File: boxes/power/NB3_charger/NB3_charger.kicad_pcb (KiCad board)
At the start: 2 copper layers, 110 x 71 mm, 40 parts, among them J1 Barrel_Jack_PJ-036AH-SMT-TR, J2 Connector_S4B-PH-SM4-TB(LF)(S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, J3 Conn_01x02_Pin, SW1 SW_SPDT, U1 Voltage_Regulator_AP64501

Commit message: Work on PCBs (v1 and v2)
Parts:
- added H10: MountingHole, MountingHole:MountingHole_2.7mm_M2.5_ISO7380_Pad, F.Cu at (209.5, 46.2)
- added H11: MountingHole, MountingHole:MountingHole_2.7mm_M2.5_ISO7380_Pad, F.Cu at (209.5, 104.2)
- added H12: MountingHole, MountingHole:MountingHole_2.7mm_M2.5_ISO7380_Pad, F.Cu at (160.5, 104.2)
- added H13: MountingHole, MountingHole:MountingHole_2.7mm_M2.5_ISO7380_Pad, F.Cu at (154.5, 46.2)
- added H14: MountingHole, MountingHole:MountingHole_2.7mm_M2.5_ISO7380_Pad, F.Cu at (215.5, 46.2)
- added H5: MountingHole, MountingHole:MountingHole_2.7mm_M2.5_ISO7380_Pad, F.Cu at (144.0, 34.2)
- added H6: MountingHole, MountingHole:MountingHole_2.7mm_M2.5_ISO7380_Pad, F.Cu at (226.0, 34.2)
- added H7: MountingHole, MountingHole:MountingHole_2.7mm_M2.5_ISO7380_Pad, F.Cu at (226.0, 116.2)
- added H8: MountingHole, MountingHole:MountingHole_2.7mm_M2.5_ISO7380_Pad, F.Cu at (144.0, 116.2)
- added H9: MountingHole, MountingHole:MountingHole_2.7mm_M2.5_ISO7380_Pad, F.Cu at (160.5, 46.2)
- BT1, BT2, BT3, BT4, BT5, BT6: moved to F.Cu
- J2: value Connector_S4B-PH-SM4-TB(LF)(SN) -> B4B-PH-K-S; footprint NB3_charger:Connector_S4B-PH-SM4-TB(LF)(SN) -> NB3_charger:Connector_B4B-PH-K-S(LF)(SN)
- moved H3 121.3 mm to (236.0, 126.2), turned to 0 degrees
- moved H1 109.8 mm to (134.0, 24.2), turned to 0 degrees
- moved H2 103.0 mm to (236.0, 24.2), turned to 0 degrees
- moved BT1 86.2 mm to (227.0, 75.2), turned to -90 degrees
- moved BT6 86.0 mm to (143.0, 75.2), turned to -90 degrees
- moved SW1 79.2 mm to (173.0, 27.2), turned to 90 degrees
- moved R1 70.7 mm to (194.1, 23.4), turned to 180 degrees
- moved R6 69.1 mm to (200.0, 23.4), turned to 0 degrees
- moved D1 69.0 mm to (196.0, 24.2), turned to -90 degrees
- moved D2 68.4 mm to (198.0, 24.2), turned to -90 degrees
- moved J3 59.4 mm to (174.6, 45.0), turned to 180 degrees
- moved J1 56.5 mm to (185.3, 38.2), turned to -90 degrees
- moved C3 53.3 mm to (183.7, 42.2), turned to 180 degrees
- moved C1 50.5 mm to (183.7, 44.7), turned to 180 degrees
- moved C4 50.3 mm to (187.2, 42.2), turned to 0 degrees
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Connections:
- J2 pad 1: GND -> +5V
- J2 pad 2: GND -> +5V
- J2 pad 3: +5V -> GND
- J2 pad 4: +5V -> GND
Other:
- board size 110 x 71 mm -> 110 x 110 mm

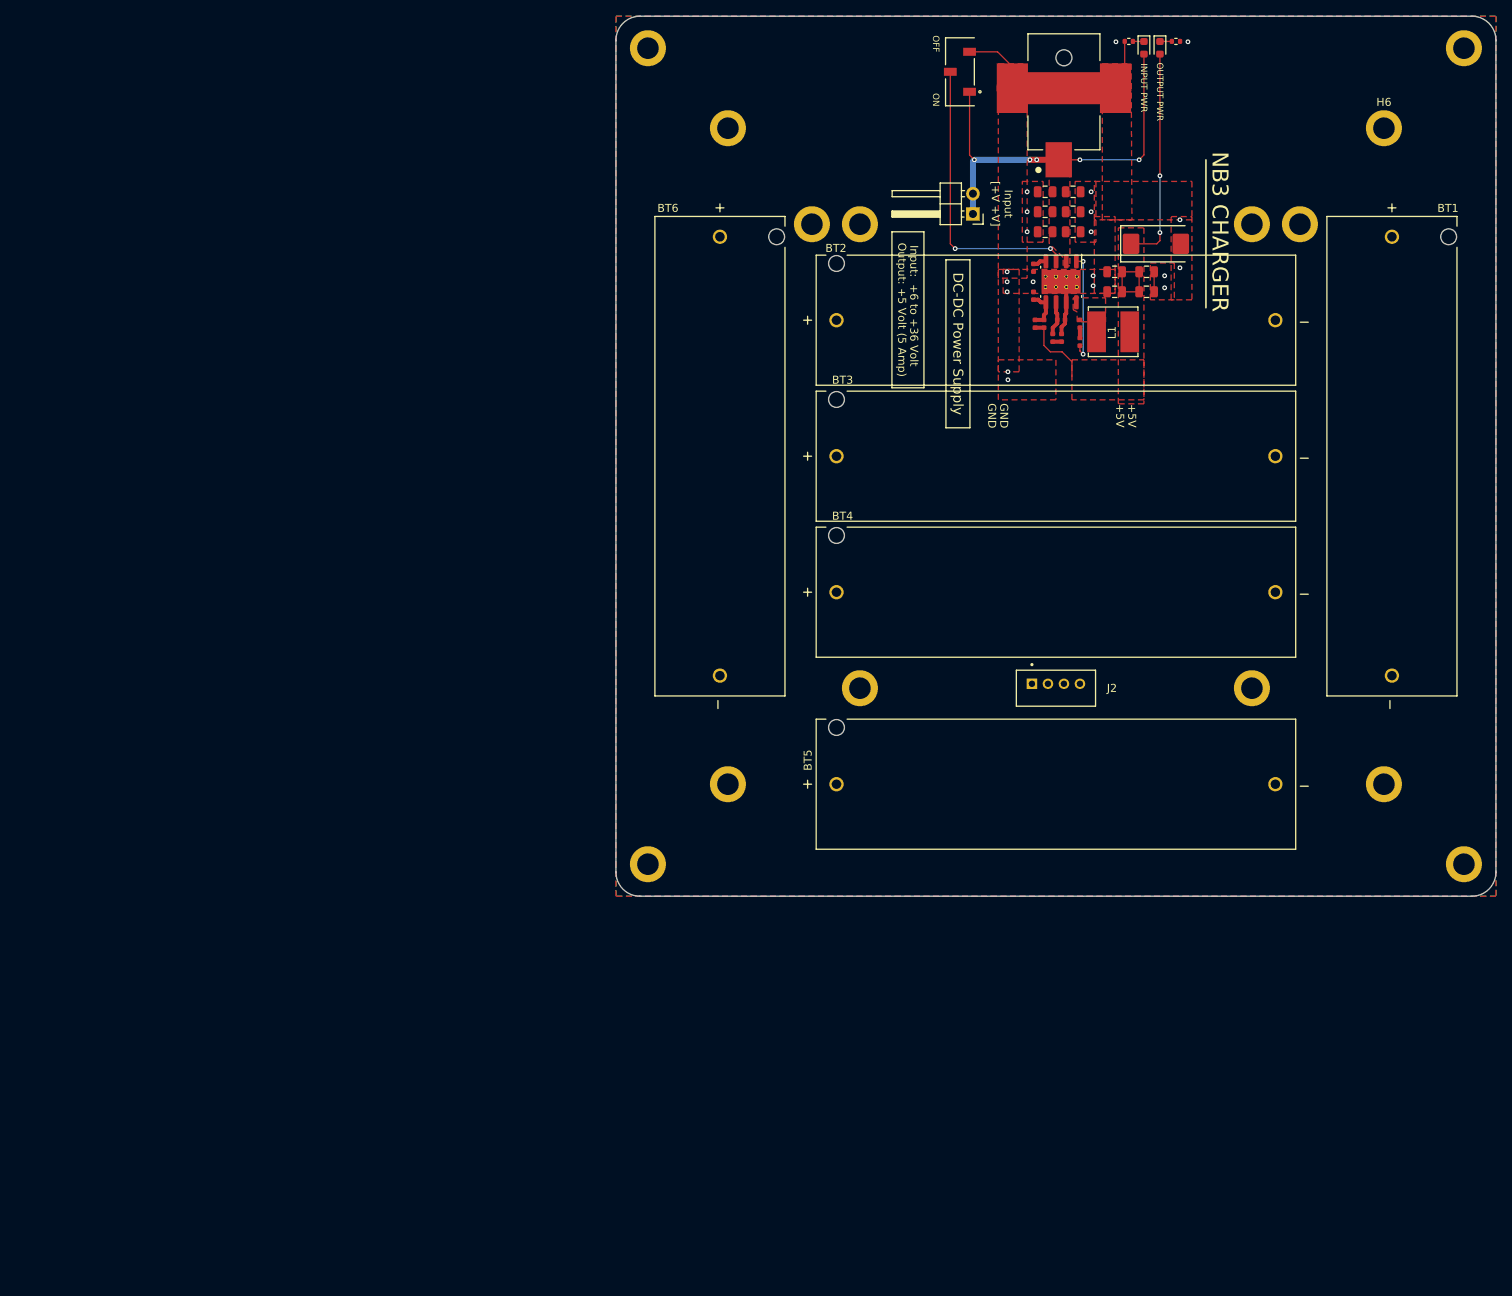
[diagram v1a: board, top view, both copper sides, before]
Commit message: PCB tweaks (charger and body)
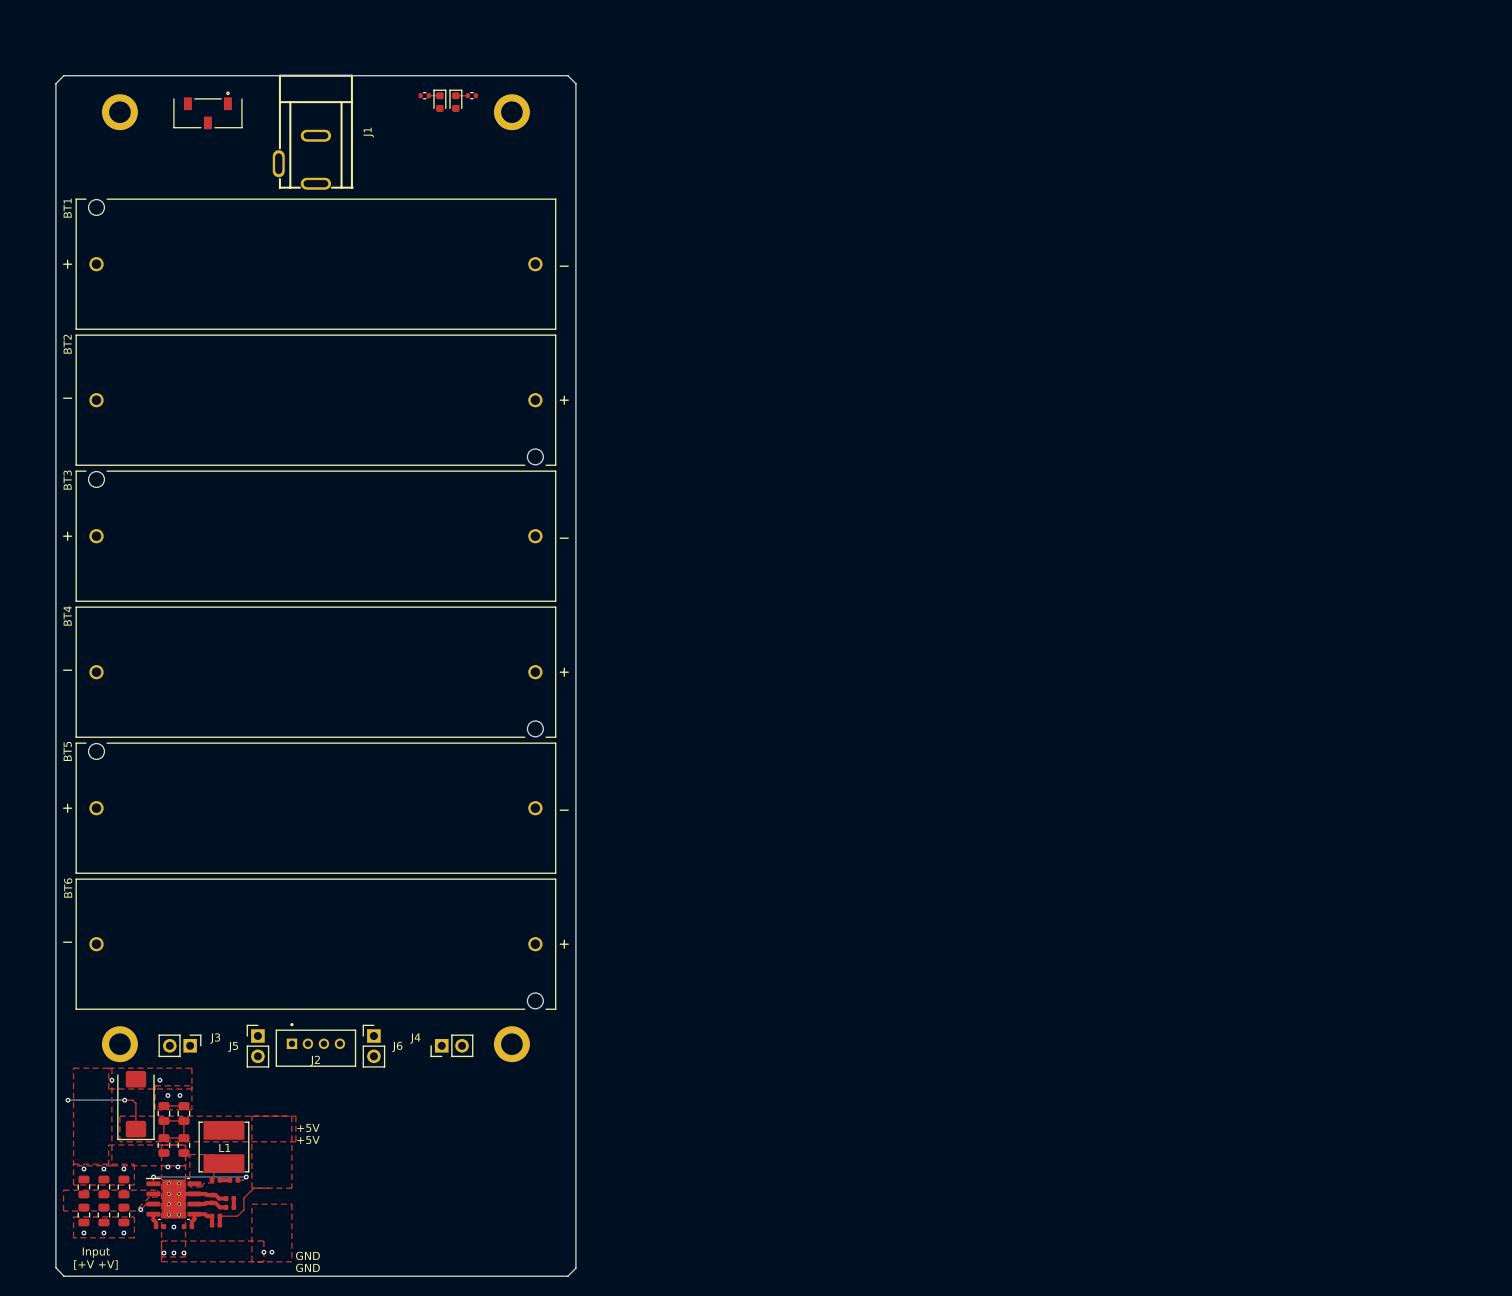
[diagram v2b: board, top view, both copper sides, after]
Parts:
- removed H1, H13, H14, H2, H3, H4, H5, H6, H7, H8: MountingHole, MountingHole:MountingHole_2.7mm_M2.5_ISO7380_Pad
- added J4: Conn_01x02_Pin, Connector_PinHeader_2.54mm:PinHeader_1x02_P2.54mm_Vertical, F.Cu at (108.2, 148.9)
- added J5: Conn_01x02_Pin, Connector_PinHeader_2.54mm:PinHeader_1x02_P2.54mm_Vertical, F.Cu at (85.2, 147.7)
- added J6: Conn_01x02_Pin, Connector_PinHeader_2.54mm:PinHeader_1x02_P2.54mm_Vertical, F.Cu at (99.8, 147.7)
- J1: value Barrel_Jack_PJ-036AH-SMT-TR -> Barrel_Jack-DC-5.5-2.1; footprint NB3_charger:Barrel_Jack_PJ-036AH-SMT-TR -> NB3_charger:Barrel_Jack_TH_XUNPU_DC-005-A200
- J3: footprint Connector_PinHeader_2.54mm:PinHeader_1x02_P2.54mm_Horizontal -> Connector_PinHeader_2.54mm:PinHeader_1x02_P2.54mm_Vertical
- moved C3 175.5 mm to (63.5, 170.1), turned to -90 degrees
- moved C4 175.4 mm to (63.5, 166.6), turned to 90 degrees
- moved C1 171.9 mm to (66.0, 170.1), turned to -90 degrees
- moved C5 171.9 mm to (66.0, 166.6), turned to 90 degrees
- moved C2 168.4 mm to (68.5, 170.1), turned to -90 degrees
- moved C6 168.3 mm to (68.5, 166.6), turned to 90 degrees
- moved C16 166.8 mm to (70.0, 156.2), turned to 90 degrees
- moved C8 162.1 mm to (73.0, 171.6), turned to 0 degrees
- moved C14 161.7 mm to (73.5, 157.4), turned to 90 degrees
- moved C13 161.4 mm to (73.5, 161.4), turned to -90 degrees
- moved U1 159.5 mm to (74.8, 168.1), turned to 0 degrees
- moved C15 158.2 mm to (76.0, 157.4), turned to 90 degrees
- moved C12 157.9 mm to (76.0, 161.4), turned to -90 degrees
- moved R5 157.2 mm to (76.5, 171.6), turned to 180 degrees
- moved C9 152.8 mm to (79.5, 168.1), turned to 90 degrees
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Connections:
- J3 pad 1: +12V -> GND
- J3 pad 2: +12V -> +5V
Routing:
- net +12V: track 50.5 -> 0.00 mm, vias 5 -> 0
- net Net-(SW1-B): track 36.1 -> 1.88 mm, vias 2 -> 1
- net GND: track 37.7 -> 9.67 mm, vias 20 -> 18
- net +5V: track 46.2 -> 31.0 mm
- removed copper zone on B.Cu, net GND
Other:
- board size 110 x 110 mm -> 65 x 150.1 mm
- board text removed: "DC-DC Power Supply"
- board text removed: "For Research and Education ONLY"
- board text removed: "INPUT PWR"
- board text removed: "Input: +6 to +36 Volt"
- board text removed: "NB3 CHARGER"
- board text removed: "NB3_charger Rev 0.0.0"
- board text removed: "OFF"
- board text removed: "ON"
- board text removed: "OUTPUT PWR"
- board text removed: "Output: +5 Volt (5 Amp)"

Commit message: Update NB3 Charger (schematic) with power path
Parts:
- removed H10, H11, H12, H9: MountingHole, MountingHole:MountingHole_2.7mm_M2.5_ISO7380_Pad
- added C17: 10uF 35v, Capacitor_SMD:C_0805_2012Metric, F.Cu at (140.6, 157.6)
- added C18: 10uF, Capacitor_SMD:C_0805_2012Metric, F.Cu at (140.6, 160.6)
- added C19: 10uF 35v, Capacitor_SMD:C_0805_2012Metric, F.Cu at (140.6, 163.6)
- added CR1: Schottky_PMEG3050EP,115, NB3_charger:Schottky_PMEG3050EP,115, F.Cu at (139.0, 168.2)
- added CR2: Schottky_PMEG3050EP,115, NB3_charger:Schottky_PMEG3050EP,115, F.Cu at (139.0, 172.6)
- added D3: LED (Green), LED_SMD:LED_0603_1608Metric, F.Cu at (144.6, 167.3)
- added H1: MountingHole, MountingHole:MountingHole_2.7mm_M2.5_ISO7380_Pad, F.Cu at (68.0, 32.2)
- added H2: MountingHole, MountingHole:MountingHole_2.7mm_M2.5_ISO7380_Pad, F.Cu at (117.0, 32.2)
- added H3: MountingHole, MountingHole:MountingHole_2.7mm_M2.5_ISO7380_Pad, F.Cu at (68.0, 148.8)
- added H4: MountingHole, MountingHole:MountingHole_2.7mm_M2.5_ISO7380_Pad, F.Cu at (117.0, 148.8)
- added Q1: PMOS_FDC658AP, NB3_charger:PMOS_SMD_FDC658AP, F.Cu at (138.3, 177.0)
- added R10: 15K 1%, Resistor_SMD:R_0402_1005Metric, F.Cu at (137.0, 163.0)
- added R11: 15K 1%, Resistor_SMD:R_0402_1005Metric, F.Cu at (137.0, 165.0)
- added R7: 5.6k, Resistor_SMD:R_0402_1005Metric, F.Cu at (137.0, 157.1)
- added R8: 3.6K 1%, Resistor_SMD:R_0402_1005Metric, F.Cu at (137.0, 159.1)
- added R9: 1.5K 1%, Resistor_SMD:R_0402_1005Metric, F.Cu at (137.0, 161.1)
- added SW2: SW_SPDT, NB3_charger:Switch_SPDT_SMD_Slide_JS102011JCQN, F.Cu at (140.5, 152.9)
- added T1: NTCG163JF103FT1, NB3_charger:Thermistor_NTC_NTCG163JF103FT1, F.Cu at (144.5, 169.9)
- added U2: BQ25172DSGR, NB3_charger:NiMH_Charger_BQ25172DSGR, F.Cu at (143.6, 176.5)
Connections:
- C1 pad 1: +12V -> VDC
- C2 pad 1: +12V -> VDC
- C3 pad 1: +12V -> VDC
- C4 pad 1: +12V -> VDC
- C5 pad 1: +12V -> VDC
- C6 pad 1: +12V -> VDC
- SW1 pad 1: +12V -> VDC
- U1 pad 2: +12V -> VDC
